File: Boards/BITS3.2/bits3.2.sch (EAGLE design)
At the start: 33 parts, among them U1 LMR16020, X1 53261-04, X2 53398-10

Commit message: Finalizing BITS v3.2
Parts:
- removed LED2: Green, led:LEDCHIP-LED0603
- removed R10: 470, resistor:R-US_R0603
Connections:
- removed net LED2: R10.1, U$2.3/CAN-TX/PWM
- removed net N$5: LED2.A, R10.2
- net GND: no longer LED2.C
- net NETAV: now also U$2.3/CAN-TX/PWM

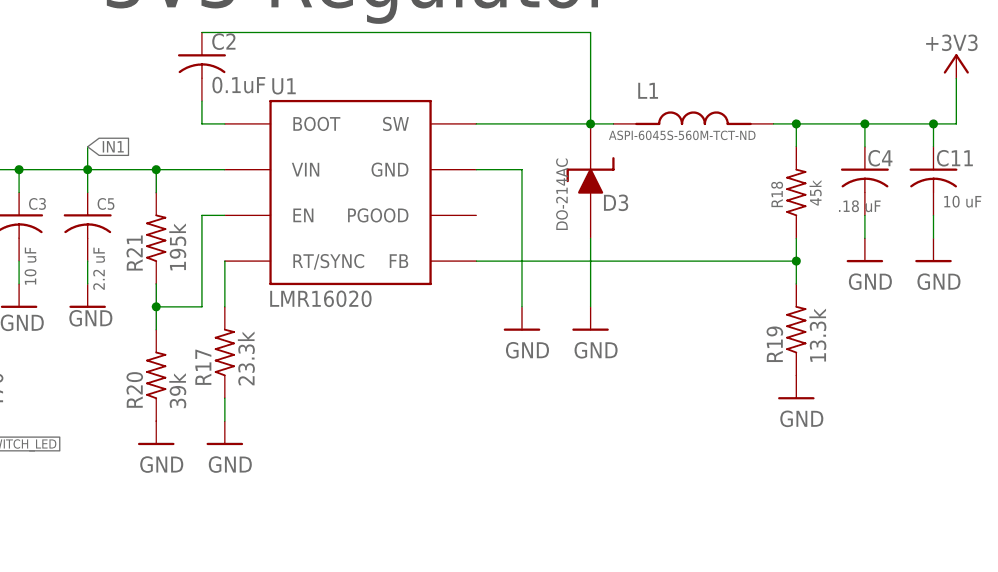
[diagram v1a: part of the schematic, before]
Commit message: Handling R values
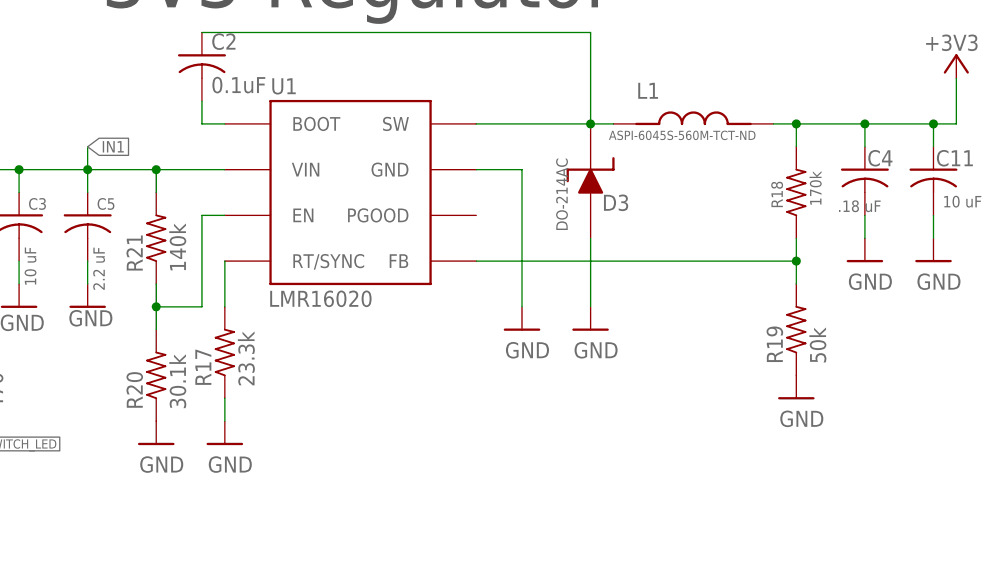
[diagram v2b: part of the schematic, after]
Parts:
- R18: value 45k -> 170k
- R19: value 13.3k -> 50k
- R20: value 39k -> 30.1k
- R21: value 195k -> 140k
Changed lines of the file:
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@@
 <part name="R17" library="resistor" deviceset="R-US_" device="R0603" value="23.3k"/>
 <part name="L1" library="inductors" deviceset="ASPI-6045S-560M-TCT-ND" device=""/>
-<part name="R18" library="resistor" deviceset="R-US_" device="R0603" value="45k"/>
-<part name="R19" library="resistor" deviceset="R-US_" device="R0603" value="13.3k"/>
+<part name="R18" library="resistor" deviceset="R-US_" device="R0603" value="170k"/>
+<part name="R19" library="resistor" deviceset="R-US_" device="R0603" value="50k"/>
 <part name="C2" library="resistor" deviceset="C-US" device="C0603" value="0.1uF"/>
 <part name="C3" library="resistor" deviceset="C-US" device="C1210" value="10 uF"/>
@@
 <part name="U1" library="HASP" deviceset="LMR16020" device=""/>
 <part name="D3" library="HASP" deviceset="DO-214AC" device=""/>
-<part name="R20" library="resistor" deviceset="R-US_" device="R0603" value="39k"/>
-<part name="R21" library="resistor" deviceset="R-US_" device="R0603" value="195k"/>
+<part name="R20" library="resistor" deviceset="R-US_" device="R0603" value="30.1k"/>
+<part name="R21" library="resistor" deviceset="R-US_" device="R0603" value="140k"/>
 <part name="SUPPLY20" library="supply1" deviceset="GND" device=""/>
 <part name="+3V3" library="supply1@1" deviceset="+3V3" device=""/>

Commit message: minor R val changes, STEP generation
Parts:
- R18: value 170k -> 340k
- R19: value 50k -> 100k
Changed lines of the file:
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@@
 <part name="R17" library="resistor" deviceset="R-US_" device="R0603" value="23.3k"/>
 <part name="L1" library="inductors" deviceset="ASPI-6045S-560M-TCT-ND" device=""/>
-<part name="R18" library="resistor" deviceset="R-US_" device="R0603" value="170k"/>
-<part name="R19" library="resistor" deviceset="R-US_" device="R0603" value="50k"/>
+<part name="R18" library="resistor" deviceset="R-US_" device="R0603" value="340k"/>
+<part name="R19" library="resistor" deviceset="R-US_" device="R0603" value="100k"/>
 <part name="C2" library="resistor" deviceset="C-US" device="C0603" value="0.1uF"/>
 <part name="C3" library="resistor" deviceset="C-US" device="C1210" value="10 uF"/>
